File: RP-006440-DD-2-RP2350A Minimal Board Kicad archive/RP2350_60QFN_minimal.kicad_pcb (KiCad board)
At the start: 2 copper layers, 52 x 51 mm, 43 parts, among them J1 USB_B_Micro, J2 Conn_02x18_Odd_Even, J3 Conn_02x18_Odd_Even, J4 SM03B-SRSS-TB, SW1 SW_Push, SW2 SW_Push, U1 RP2350_60QFN, U2 NCP1117-3.3_SOT223, U3 W25Q128JVS, Y1 ABM8-272-T3

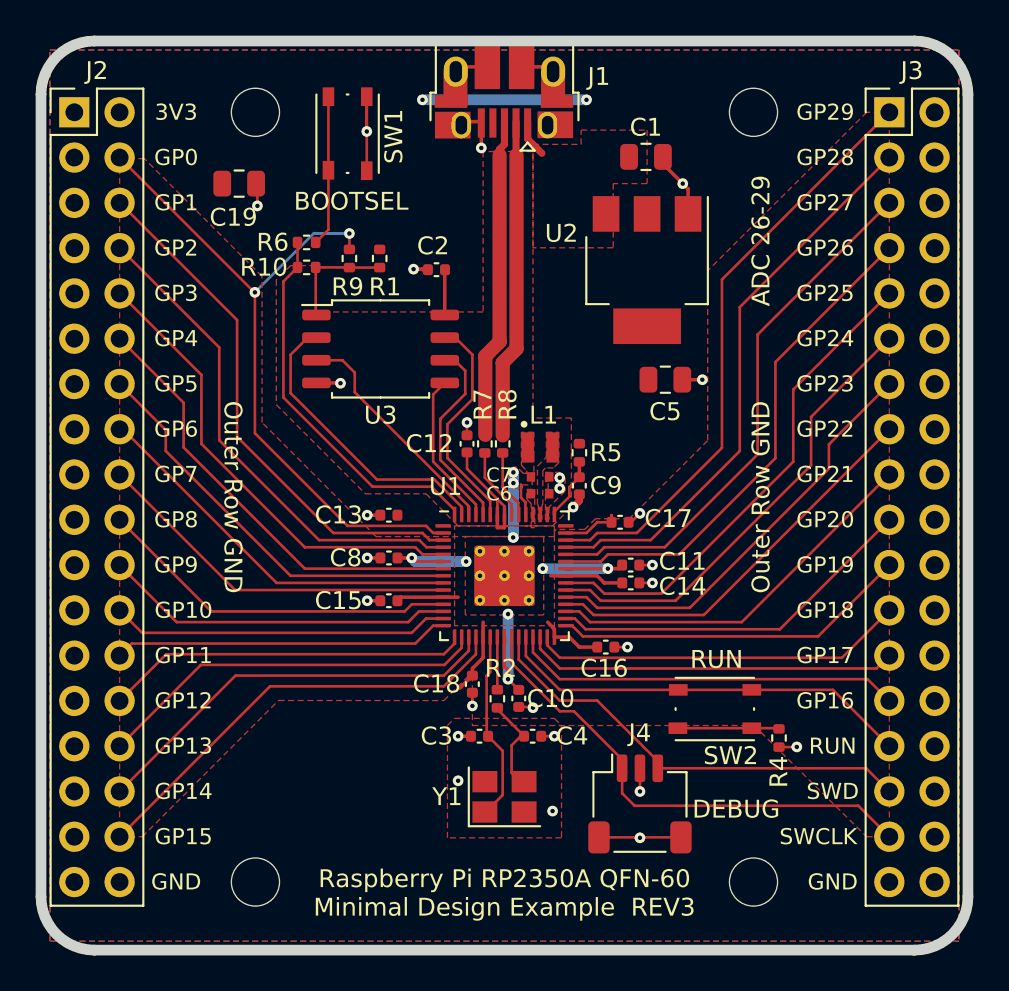
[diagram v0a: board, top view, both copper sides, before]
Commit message: Update PCB
added usbc receptacle and resistor footprints to pcb
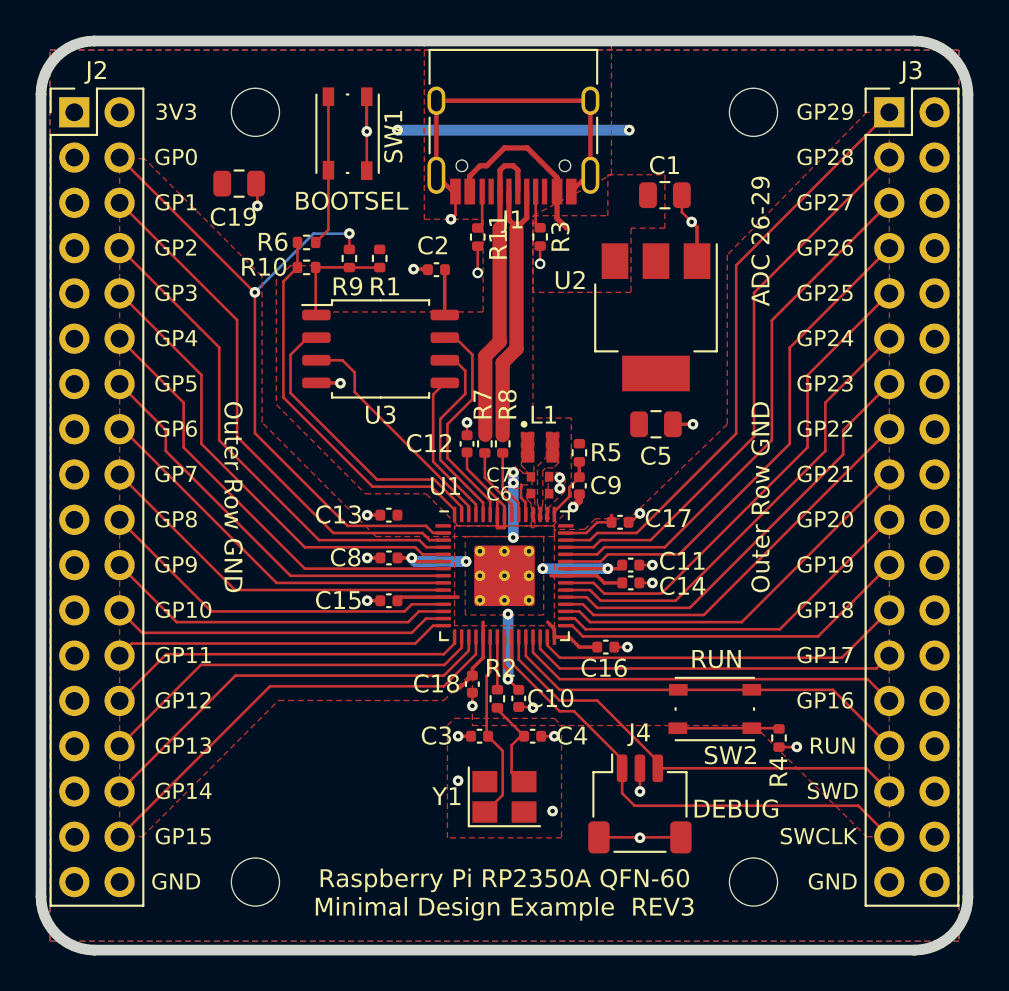
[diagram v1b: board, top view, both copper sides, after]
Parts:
- added R11: 5.1K, Resistor_SMD:R_0402_1005Metric, F.Cu at (98.5, 81.0)
- added R3: 5.1K, Resistor_SMD:R_0402_1005Metric, F.Cu at (102.0, 81.0)
- J1: value USB_B_Micro -> USB_C_Receptacle_USB2.0_16P; footprint Connector_USB:USB_Micro-B_Amphenol_10103594-0001LF_Horizontal -> Connector_USB:USB_C_Receptacle_HRO_TYPE-C-31-M-12
- moved U2 2.70 mm to (108.5, 85.5)
- moved C5 2.55 mm to (108.5, 91.5)
- moved C1 2.40 mm to (109.0, 78.7)
- moved J1 1.65 mm to (100.5, 74.4)
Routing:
- net GND: track 37.5 -> 54.9 mm, vias 27 -> 29
- net VBUS: track 2.11 -> 10.2 mm
- net +3V3: track 37.6 -> 41.4 mm
- net Net-(J1-CC2): track 0.00 -> 2.15 mm
- net Net-(J1-CC1): track 0.00 -> 2.14 mm
- net /USB_D-: track 17.9 -> 16.5 mm
